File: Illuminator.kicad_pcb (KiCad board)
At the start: 2 copper layers, 13 parts, among them Q0 BSN20

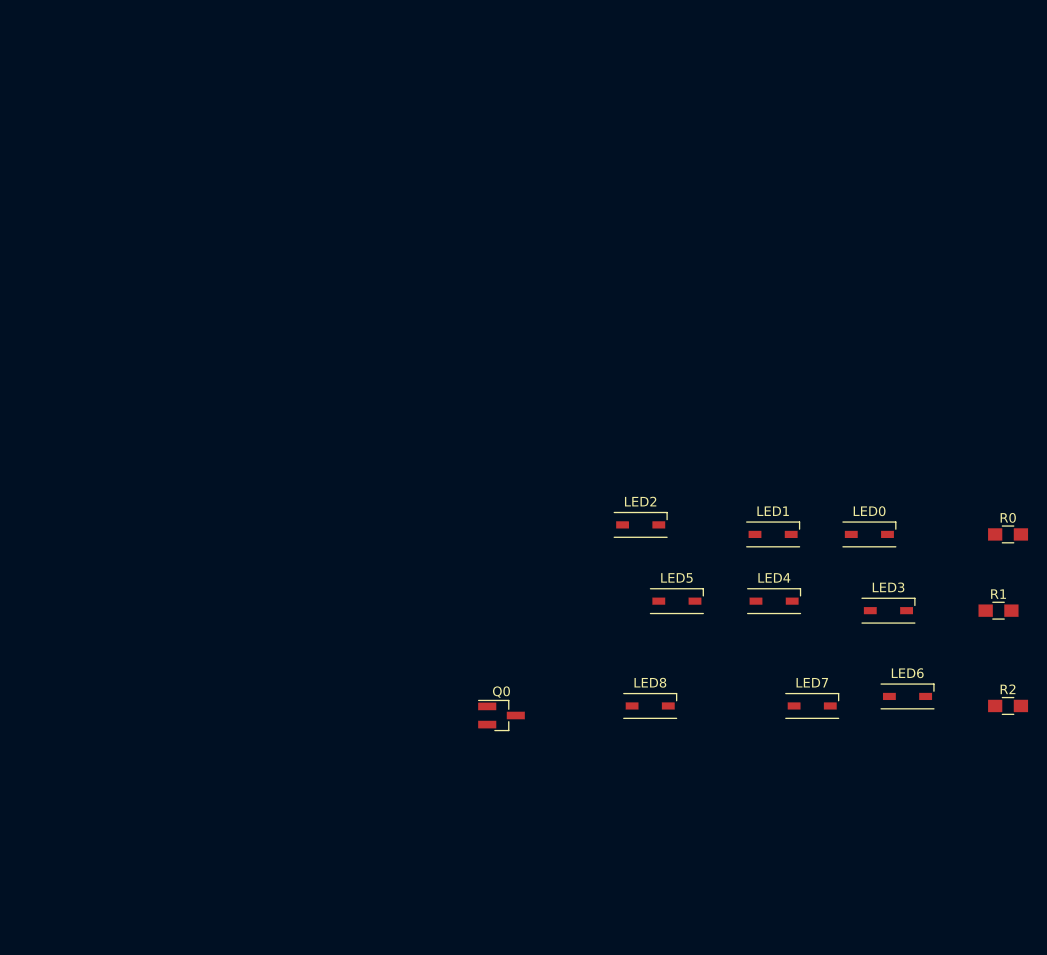
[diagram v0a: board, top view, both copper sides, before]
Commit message: Applying the synthesizing script to the PCB
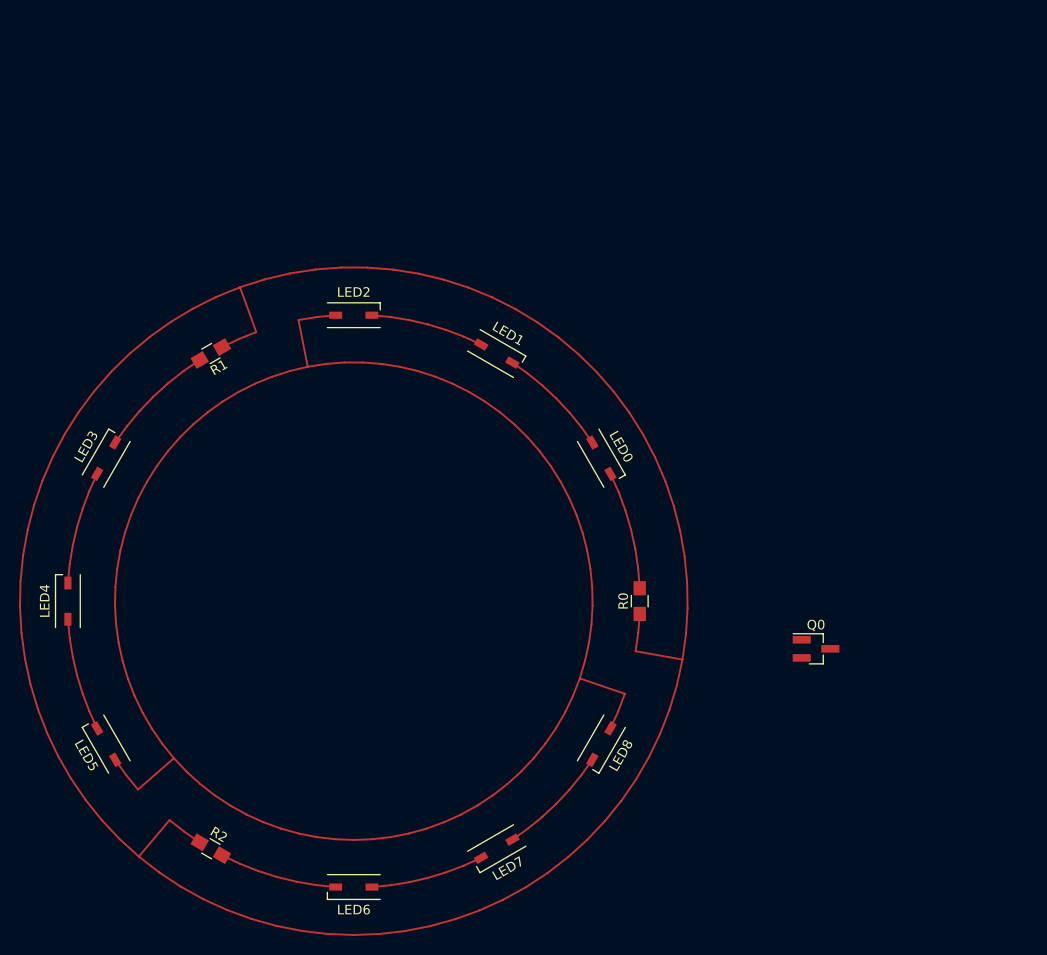
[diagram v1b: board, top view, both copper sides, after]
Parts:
- moved R1 86.9 mm to (85.0, 74.0), turned to 210 degrees
- moved R2 85.0 mm to (85.0, 126.0), turned to 330 degrees
- moved LED3 83.6 mm to (74.0, 85.0), turned to 60 degrees
- moved LED4 74.1 mm to (70.0, 100.0), turned to 90 degrees
- moved LED5 61.7 mm to (74.0, 115.0), turned to 120 degrees
- moved LED6 61.4 mm to (100.0, 130.0), turned to 180 degrees
- moved R0 39.3 mm to (130.0, 100.0), turned to 90 degrees
- moved LED2 37.3 mm to (100.0, 70.0)
- moved LED7 36.3 mm to (115.0, 126.0), turned to 210 degrees
- moved LED1 34.7 mm to (115.0, 74.0), turned to 330 degrees
- moved Q0 33.7 mm to (148.5, 105.0)
- moved LED0 29.2 mm to (126.0, 85.0), turned to 300 degrees
- moved LED8 6.50 mm to (126.0, 115.0), turned to 240 degrees
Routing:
- net +5V: track 0.00 -> 246.8 mm
- net Net-(LED2-Pad1): track 0.00 -> 184.2 mm
- net Net-(LED3-Pad2): track 0.00 -> 12.5 mm
- net Net-(LED6-Pad2): track 0.00 -> 12.5 mm
- net Net-(LED0-Pad2): track 0.00 -> 12.5 mm
- net Net-(LED0-Pad1): track 0.00 -> 11.9 mm
- net Net-(LED7-Pad1): track 0.00 -> 11.9 mm
- net Net-(LED4-Pad1): track 0.00 -> 11.9 mm
- net Net-(LED1-Pad1): track 0.00 -> 11.9 mm
- net Net-(LED6-Pad1): track 0.00 -> 11.9 mm
- net Net-(LED3-Pad1): track 0.00 -> 11.9 mm

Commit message: Possible placement for mosfet
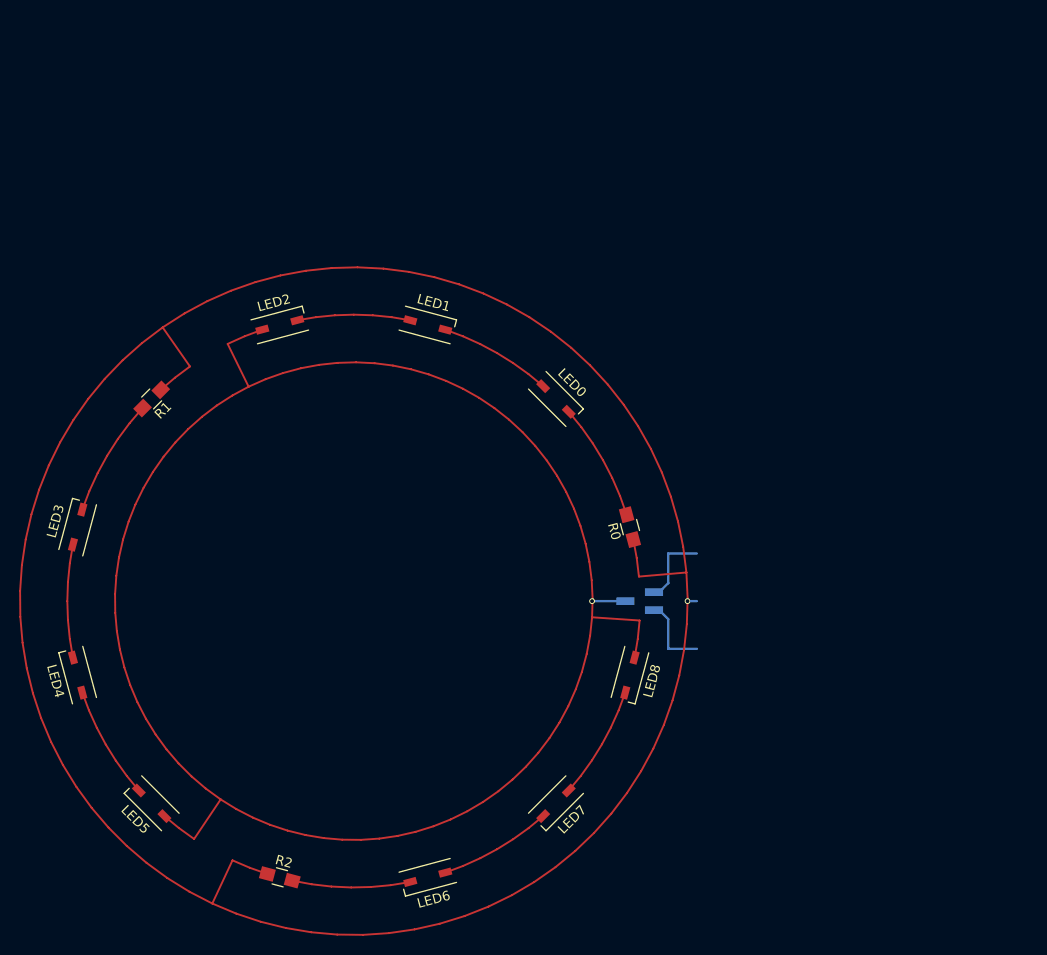
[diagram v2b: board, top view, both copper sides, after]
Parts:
- Q0: moved to B.Cu
- moved Q0 19.2 mm to (130.0, 100.0), turned to 180 degrees
- moved R0 7.83 mm to (129.0, 92.2), turned to 105 degrees
- moved LED0 7.83 mm to (121.2, 78.8), turned to 315 degrees
- moved R1 7.83 mm to (78.8, 78.8), turned to 225 degrees
- moved LED5 7.83 mm to (78.8, 121.2), turned to 135 degrees
- moved LED2 7.83 mm to (92.2, 71.0), turned to 15 degrees
- moved LED4 7.83 mm to (71.0, 107.8), turned to 105 degrees
- moved R2 7.83 mm to (92.2, 129.0), turned to 345 degrees
- moved LED1 7.83 mm to (107.8, 71.0), turned to 345 degrees
- moved LED3 7.83 mm to (71.0, 92.2), turned to 75 degrees
- moved LED7 7.83 mm to (121.2, 121.2), turned to 225 degrees
- moved LED6 7.83 mm to (107.8, 129.0), turned to 195 degrees
- moved LED8 7.83 mm to (129.0, 107.8), turned to 255 degrees
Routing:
- net GND: track 0.00 -> 7.99 mm
- net +3V3: track 0.00 -> 7.99 mm
- net Net-(LED2-Pad1): track 184.2 -> 187.7 mm, vias 0 -> 1
- net +5V: track 246.8 -> 247.8 mm, vias 0 -> 1

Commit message: Committing changes to PCB due to synthesize.py
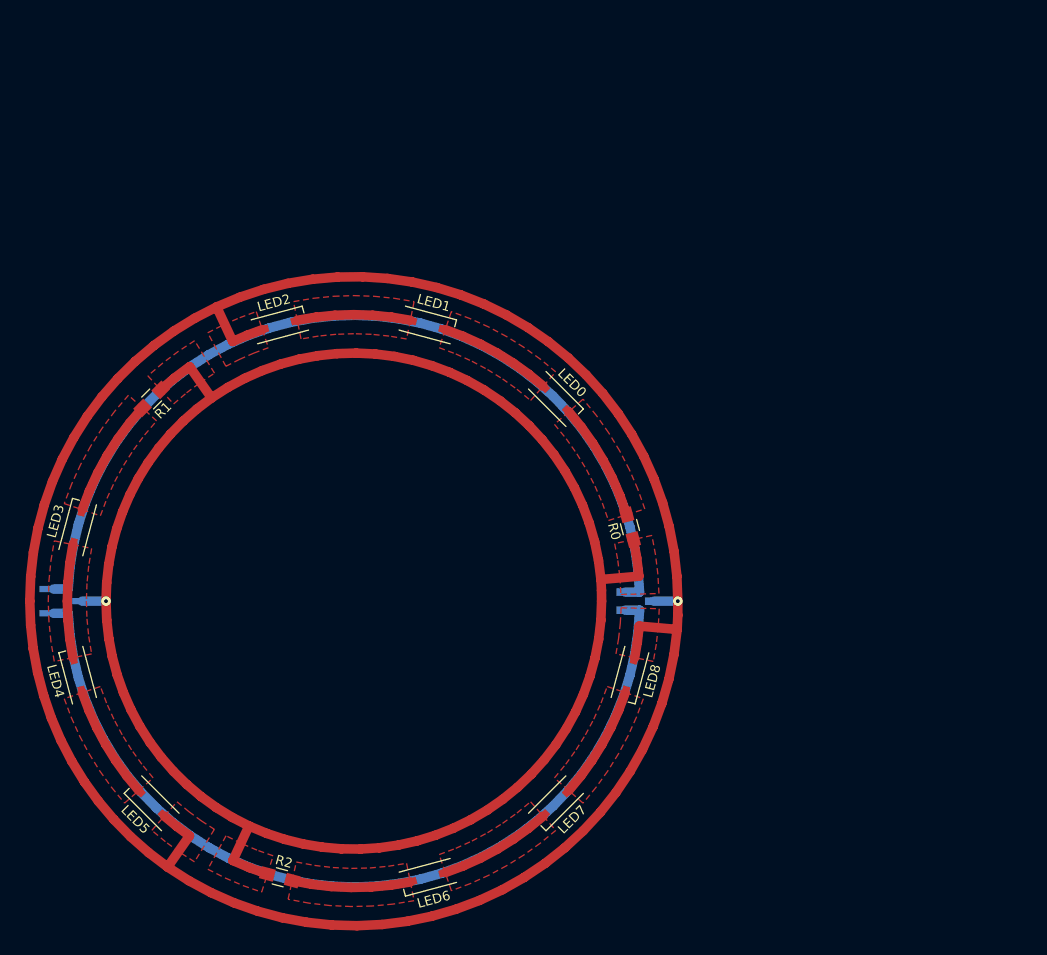
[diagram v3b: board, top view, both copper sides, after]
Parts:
- added J0: Conn_01x03_Male, Pin_Headers:Pin_Header_Straight_1x03_Pitch1.27mm_SMD_Pin1Left, B.Cu at (70.0, 100.0)
- turned Q0 to 0 degrees
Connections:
- net +5V renamed /TO_5V
- Q0 pad 1: +3V3 -> /TO_3V3
- Q0 pad 2: GND -> /TO_GND
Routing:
- net /TO_GND: track 0.00 -> 95.0 mm
- net /TO_3V3: track 0.00 -> 95.0 mm
- net /TO_5V: track 247.8 -> 189.6 mm
- net Net-(LED2-Pad1): track 187.7 -> 238.4 mm
- net GND: track 7.99 -> 0.00 mm
- net +3V3: track 7.99 -> 0.00 mm
- added copper zone on F.Cu, net /TO_5V
- added copper zone on F.Cu, net Net-(LED0-Pad1)
- added copper zone on F.Cu, net Net-(LED0-Pad2)
- added copper zone on F.Cu, net Net-(LED1-Pad1)
- added copper zone on F.Cu, net Net-(LED2-Pad1)
- added copper zone on F.Cu, net Net-(LED3-Pad1)
- added copper zone on F.Cu, net Net-(LED3-Pad2)
- added copper zone on F.Cu, net Net-(LED4-Pad1)
- added copper zone on F.Cu, net Net-(LED6-Pad1)
- added copper zone on F.Cu, net Net-(LED6-Pad2)
- added copper zone on F.Cu, net Net-(LED7-Pad1)
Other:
- net class Default: via_dia 0.6 -> 0.8

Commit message: Filletting the big pads
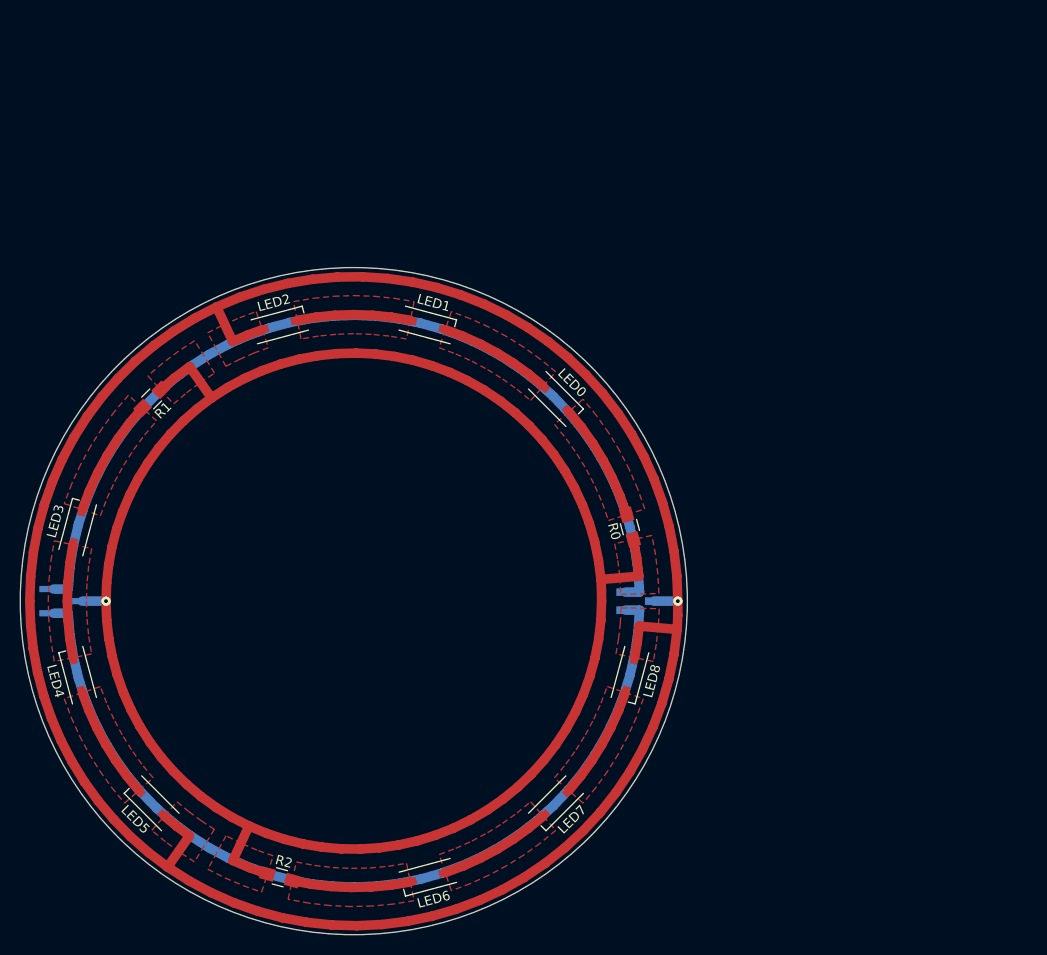
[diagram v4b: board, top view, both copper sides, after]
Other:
- board outline added: 70 x 70 mm
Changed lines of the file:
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@@
 (general
   (thickness 1.6)
-  (drawings 0)
+  (drawings 1)
   (tracks 326)
   (zones 0)
@@
 (general
   (thickness 1.6)
-  (drawings 0)
+  (drawings 1)
   (tracks 326)
   (zones 0)
@@
     )
   )
+  (gr_circle (center 100 100) (end 135 100) (layer Edge.Cuts) (width 0.1))
   (segment (start 74 100) (end 71.5 100) (width 1) (layer B.Cu) (net 1))
   (via (at 74 100) (size 1) (layers F.Cu B.Cu) (net 1))
@@
     (connect_pads yes (clearance 0.508))
     (min_thickness 0.254)
-    (fill yes (arc_segments 16) (thermal_gap 0.508) (thermal_bridge_width 0.508))
+    (fill yes (arc_segments 16) (thermal_gap 0.508) (thermal_bridge_width 0.508) (smoothing fillet) (radius 0.5))
     (polygon
       (pts
@@
     (connect_pads yes (clearance 0.508))
     (min_thickness 0.254)
-    (fill yes (arc_segments 16) (thermal_gap 0.508) (thermal_bridge_width 0.508))
+    (fill yes (arc_segments 16) (thermal_gap 0.508) (thermal_bridge_width 0.508) (smoothing fillet) (radius 0.5))
     (polygon
       (pts
@@
     (connect_pads yes (clearance 0.508))
     (min_thickness 0.254)
-    (fill yes (arc_segments 16) (thermal_gap 0.508) (thermal_bridge_width 0.508))
+    (fill yes (arc_segments 16) (thermal_gap 0.508) (thermal_bridge_width 0.508) (smoothing fillet) (radius 0.5))
     (polygon
       (pts
@@
     (connect_pads yes (clearance 0.508))
     (min_thickness 0.254)
-    (fill yes (arc_segments 16) (thermal_gap 0.508) (thermal_bridge_width 0.508))
+    (fill yes (arc_segments 16) (thermal_gap 0.508) (thermal_bridge_width 0.508) (smoothing fillet) (radius 0.5))
     (polygon
       (pts
@@
     (connect_pads yes (clearance 0.508))
     (min_thickness 0.254)
-    (fill yes (arc_segments 16) (thermal_gap 0.508) (thermal_bridge_width 0.508))
+    (fill yes (arc_segments 16) (thermal_gap 0.508) (thermal_bridge_width 0.508) (smoothing fillet) (radius 0.5))
     (polygon
       (pts
@@
     (connect_pads yes (clearance 0.508))
     (min_thickness 0.254)
-    (fill yes (arc_segments 16) (thermal_gap 0.508) (thermal_bridge_width 0.508))
+    (fill yes (arc_segments 16) (thermal_gap 0.508) (thermal_bridge_width 0.508) (smoothing fillet) (radius 0.5))
     (polygon
       (pts
@@
     (connect_pads yes (clearance 0.508))
     (min_thickness 0.254)
-    (fill yes (arc_segments 16) (thermal_gap 0.508) (thermal_bridge_width 0.508))
+    (fill yes (arc_segments 16) (thermal_gap 0.508) (thermal_bridge_width 0.508) (smoothing fillet) (radius 0.5))
     (polygon
       (pts
@@
     (connect_pads yes (clearance 0.508))
     (min_thickness 0.254)
-    (fill yes (arc_segments 16) (thermal_gap 0.508) (thermal_bridge_width 0.508))
+    (fill yes (arc_segments 16) (thermal_gap 0.508) (thermal_bridge_width 0.508) (smoothing fillet) (radius 0.5))
     (polygon
       (pts
@@
     (connect_pads yes (clearance 0.508))
     (min_thickness 0.254)
-    (fill yes (arc_segments 16) (thermal_gap 0.508) (thermal_bridge_width 0.508))
+    (fill yes (arc_segments 16) (thermal_gap 0.508) (thermal_bridge_width 0.508) (smoothing fillet) (radius 0.5))
     (polygon
       (pts
@@
     (connect_pads yes (clearance 0.508))
     (min_thickness 0.254)
-    (fill yes (arc_segments 16) (thermal_gap 0.508) (thermal_bridge_width 0.508))
+    (fill yes (arc_segments 16) (thermal_gap 0.508) (thermal_bridge_width 0.508) (smoothing fillet) (radius 0.5))
     (polygon
       (pts
@@
     (connect_pads yes (clearance 0.508))
     (min_thickness 0.254)
-    (fill yes (arc_segments 16) (thermal_gap 0.508) (thermal_bridge_width 0.508))
+    (fill yes (arc_segments 16) (thermal_gap 0.508) (thermal_bridge_width 0.508) (smoothing fillet) (radius 0.5))
     (polygon
       (pts
@@
     (connect_pads yes (clearance 0.508))
     (min_thickness 0.254)
-    (fill yes (arc_segments 16) (thermal_gap 0.508) (thermal_bridge_width 0.508))
+    (fill yes (arc_segments 16) (thermal_gap 0.508) (thermal_bridge_width 0.508) (smoothing fillet) (radius 0.5))
     (polygon
       (pts
@@
     (connect_pads yes (clearance 0.508))
     (min_thickness 0.254)
-    (fill yes (arc_segments 16) (thermal_gap 0.508) (thermal_bridge_width 0.508))
+    (fill yes (arc_segments 16) (thermal_gap 0.508) (thermal_bridge_width 0.508) (smoothing fillet) (radius 0.5))
     (polygon
       (pts
@@
     (connect_pads yes (clearance 0.508))
     (min_thickness 0.254)
-    (fill yes (arc_segments 16) (thermal_gap 0.508) (thermal_bridge_width 0.508))
+    (fill yes (arc_segments 16) (thermal_gap 0.508) (thermal_bridge_width 0.508) (smoothing fillet) (radius 0.5))
     (polygon
       (pts
@@
     (connect_pads yes (clearance 0.508))
     (min_thickness 0.254)
-    (fill yes (arc_segments 16) (thermal_gap 0.508) (thermal_bridge_width 0.508))
-    (polygon
-      (pts
+    (fill yes (arc_segments 16) (thermal_gap 0.508) (thermal_bridge_width 0.508) (smoothing fillet) (radius 0.5))
+    (polygon
+      (pts
